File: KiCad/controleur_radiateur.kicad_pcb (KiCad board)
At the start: 2 copper layers, 26 parts, among them J1 ZFKDS_3, U1 SIM800L, U2 MOC3023M, U3 MOC3023M, U4 DS18B20, U5 IRM-10-5

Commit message: [MAJ] modification pour les libs
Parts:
- A1: footprint librairie:Arduino_Nano_step -> perso:Arduino_Nano_step
- J1: footprint librairie:ZFKDS_3 -> perso:ZFKDS_3
- U1: footprint librairie:SIM800L_module -> perso:SIM800L_module
- U2, U3: footprint MOC3023M:DIP762W51P254L851H508Q6N -> perso:MOC3023M
- U5: footprint IRM-10-5:IRM-10-5 -> perso:IRM-10-5

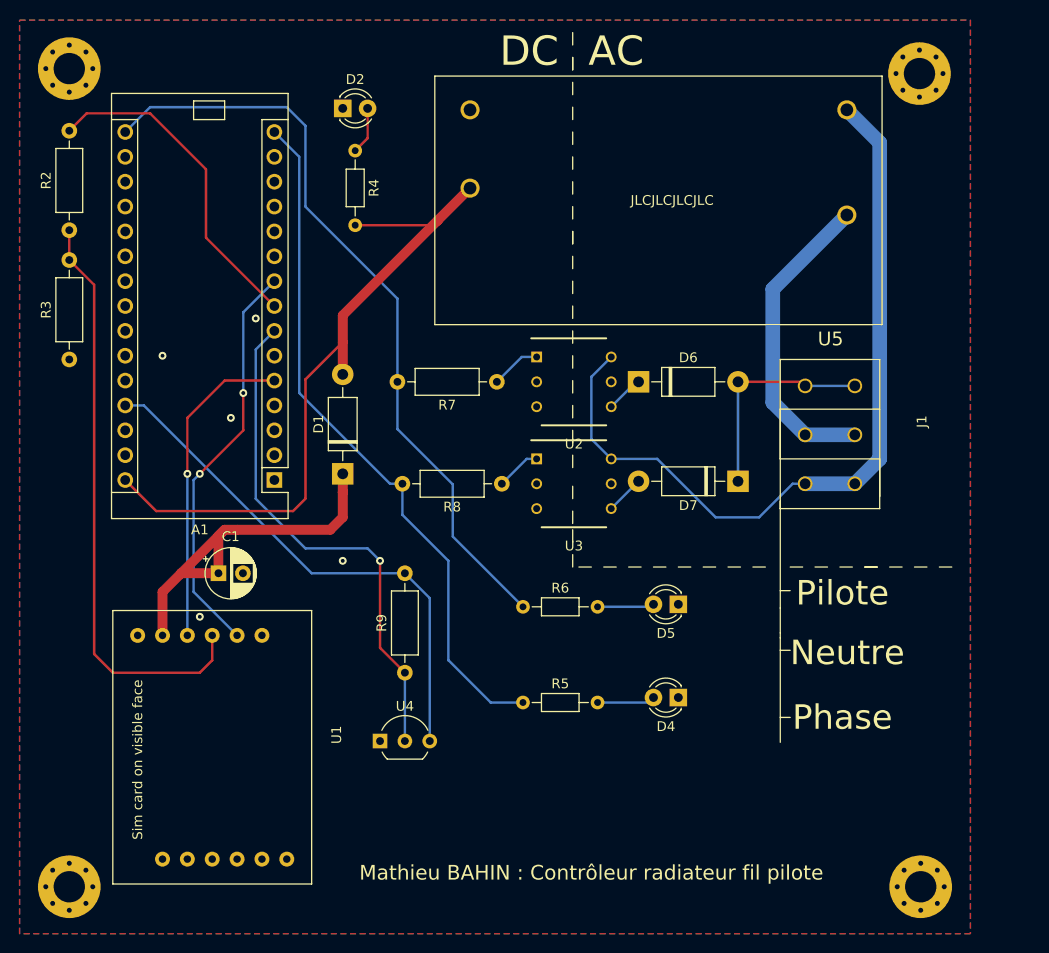
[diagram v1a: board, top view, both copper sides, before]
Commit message: PCB : suppression des led, changement optocoupleurs pour des MOC3043M, redesign du PCB Soft : reconnection automatique toutes les 1 minutes au réseau GSM
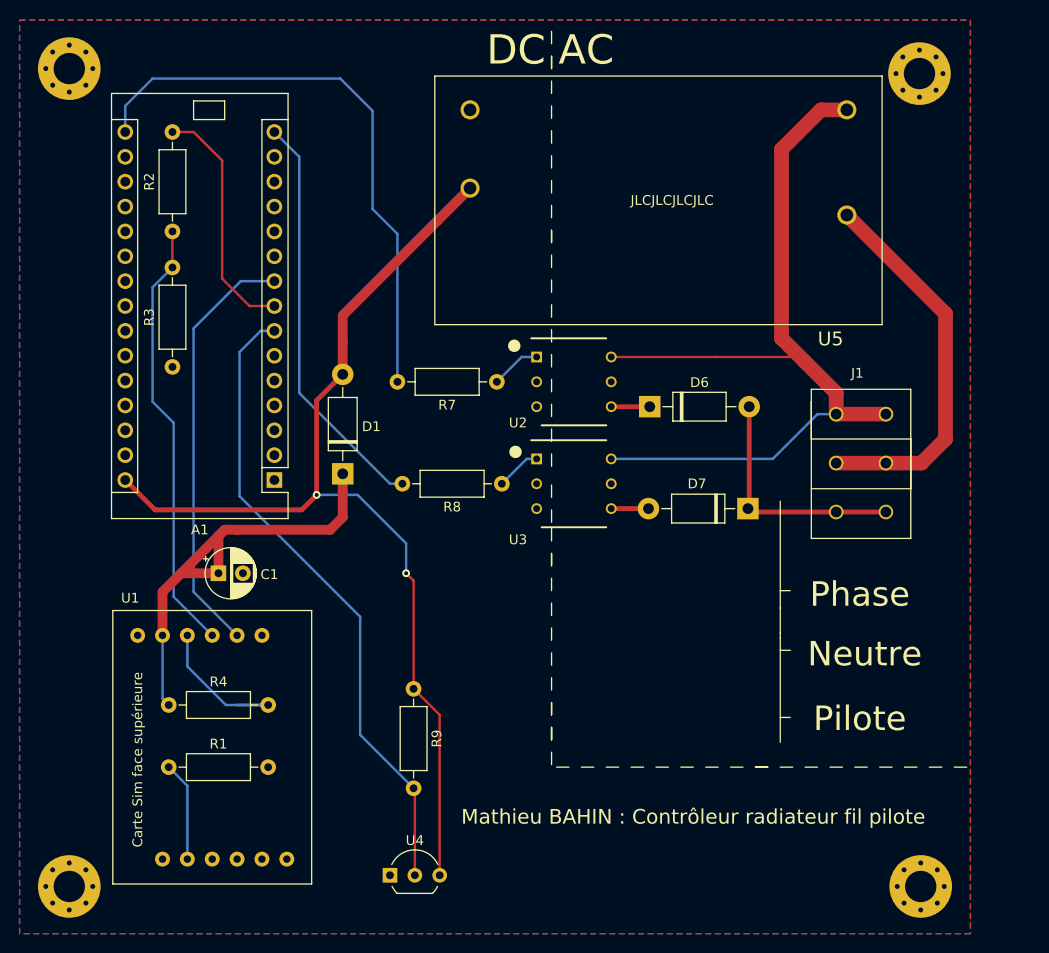
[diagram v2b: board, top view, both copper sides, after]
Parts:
- removed D2, D4, D5: LED, LED_THT:LED_D3.0mm
- removed R5, R6: 330, Resistor_THT:R_Axial_DIN0204_L3.6mm_D1.6mm_P7.62mm_Horizontal
- removed the REF** at (104.1, 147.6)
- removed the REF** at (191.1, 147.6)
- added R1: 4.7k, Resistor_THT:R_Axial_DIN0207_L6.3mm_D2.5mm_P10.16mm_Horizontal, F.Cu at (114.3, 135.4)
- added REF**: MountingHole_3.2mm_M3_Pad_Via, MountingHole:MountingHole_3.2mm_M3_Pad_Via, F.Cu at (191.1, 147.6)
- added REF**: MountingHole_3.2mm_M3_Pad_Via, MountingHole:MountingHole_3.2mm_M3_Pad_Via, F.Cu at (104.1, 147.6)
- C1: value 100u -> 100u 10V
- R4: value 330 -> 4.7k; footprint Resistor_THT:R_Axial_DIN0204_L3.6mm_D1.6mm_P7.62mm_Horizontal -> Resistor_THT:R_Axial_DIN0207_L6.3mm_D2.5mm_P10.16mm_Horizontal
- moved R4 59.8 mm to (114.3, 129.0), turned to 0 degrees
- moved U4 13.8 mm to (136.9, 146.4)
- moved J1 10.9 mm to (187.6, 99.3), turned to 270 degrees
- moved R3 10.6 mm to (114.7, 94.5)
- moved R2 10.5 mm to (114.7, 80.6)
- moved D7 2.97 mm to (173.5, 109.0)
- moved D6 2.79 mm to (163.4, 98.6)
- moved R9 1.88 mm to (139.3, 127.4), turned to 270 degrees
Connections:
- net Net-(A1-Pad15) renamed /D12
- net Net-(A1-Pad16) renamed /D13
- net Net-(A1-Pad9) renamed /TX_GSM
- net Net-(R2-Pad1) renamed /RX_GSM
- A1 pad 30: Net-(A1-Pad30) -> +5V
- A1 pad 7: Net-(A1-Pad7) -> /Temp_Data
- D1 pad 2: Net-(A1-Pad30) -> +5V
- R4 pad 1: Net-(D2-Pad2) -> Net-(C1-Pad1)
- R4 pad 2: Net-(A1-Pad30) -> Net-(R4-Pad2)
- R9 pad 1: Net-(A1-Pad7) -> +5V
- R9 pad 2: Net-(A1-Pad27) -> /Temp_Data
- REF** pad 1: GND -> (no net) (x2)
- U1 pad 3: Net-(A1-Pad5) -> Net-(R4-Pad2)
- U4 pad 2: Net-(A1-Pad7) -> /Temp_Data
- U4 pad 3: Net-(A1-Pad27) -> +5V
- U5 pad 4: Net-(A1-Pad30) -> +5V
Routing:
- net +5V: track 0.00 -> 106.5 mm, vias 0 -> 2
- net Net-(A1-Pad30): track 70.9 -> 0.00 mm
- net /Temp_Data: track 0.00 -> 65.3 mm
- net Net-(A1-Pad27): track 53.9 -> 0.00 mm
- net Net-(A1-Pad7): track 52.7 -> 0.00 mm, vias 1 -> 0
- net Net-(A1-Pad5): track 32.7 -> 0.00 mm, vias 1 -> 0
- net /D12: track 71.5 -> 42.1 mm
- net /D13: track 78.6 -> 59.2 mm
- net Net-(R4-Pad2): track 0.00 -> 16.2 mm
- net /RX_GSM: track 60.3 -> 44.6 mm
- net Net-(R1-Pad1): track 0.00 -> 10.2 mm
- net Net-(A1-Pad8): track 33.9 -> 24.8 mm
- net Net-(C1-Pad1): track 39.1 -> 46.5 mm
- net Net-(J1-Pad3): track 32.0 -> 39.3 mm
- net Net-(J1-Pad1): track 81.5 -> 87.7 mm
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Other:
- board text added: "DC AC"
- board text removed: "AC"
- board text removed: "DC"
